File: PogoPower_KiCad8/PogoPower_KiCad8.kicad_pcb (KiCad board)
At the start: 2 copper layers, 16.2 x 23.2 mm, 6 parts, among them J1 Conn_01x01, J2 Conn_01x01, J3 Conn_01x01, J4 Conn_01x01, J5 Conn_01x01, J8 Conn_02x04_Odd_Even

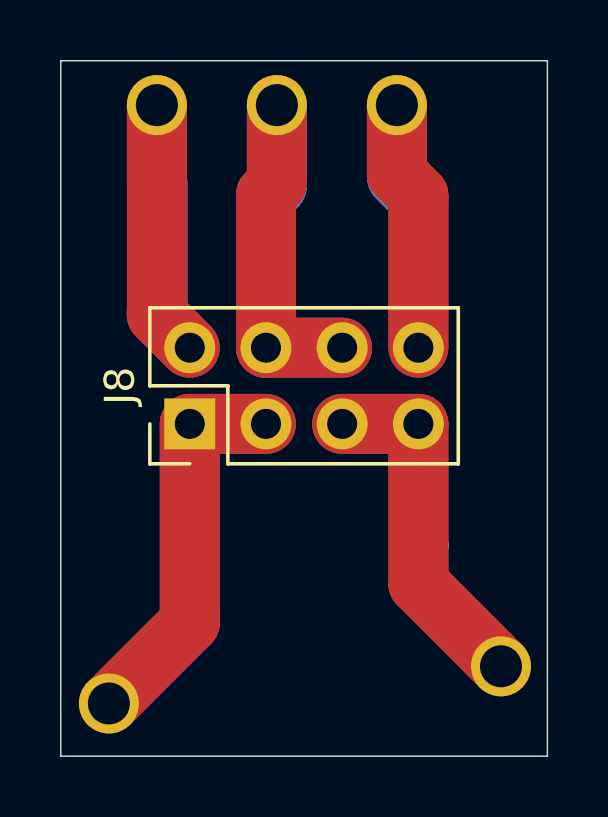
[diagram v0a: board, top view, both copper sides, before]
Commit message: Pogo Power slikscreen
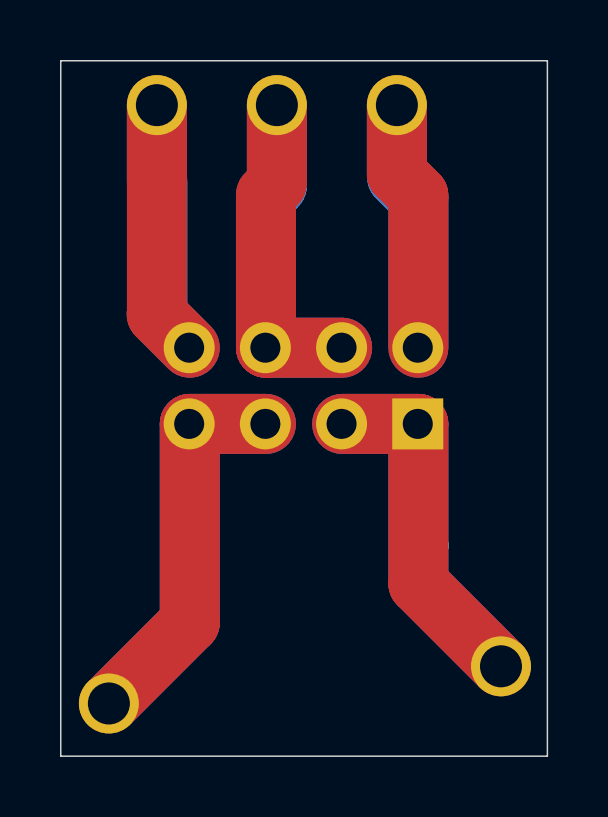
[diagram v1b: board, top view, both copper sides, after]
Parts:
- J8: moved to B.Cu
- moved J8 7.60 mm to (167.5, 115.4)
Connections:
- J8 pad 1: Net-(J1-Pin_1) -> Net-(J2-Pin_1)
- J8 pad 2: Net-(J5-Pin_1) -> Net-(J3-Pin_1)
- J8 pad 3: Net-(J1-Pin_1) -> Net-(J2-Pin_1)
- J8 pad 5: Net-(J2-Pin_1) -> Net-(J1-Pin_1)
- J8 pad 7: Net-(J2-Pin_1) -> Net-(J1-Pin_1)
- J8 pad 8: Net-(J3-Pin_1) -> Net-(J5-Pin_1)
